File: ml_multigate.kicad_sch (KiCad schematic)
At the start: 3 parts, among them U1 4001, U2 1, U2 4001

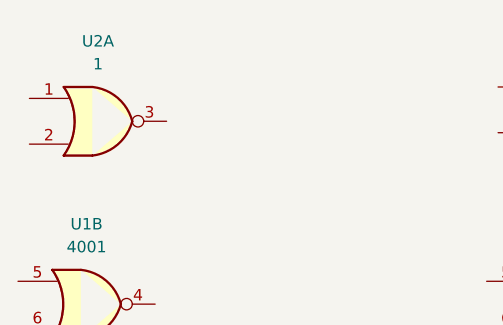
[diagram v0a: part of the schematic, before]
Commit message: Update ml_multigate.kicad_sch
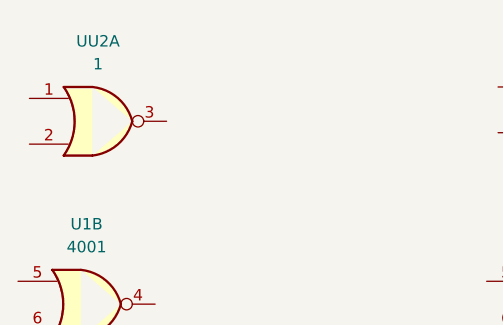
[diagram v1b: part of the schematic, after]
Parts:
- renumbered U2 to UU2
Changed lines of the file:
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@@
 		(dnp no)
 		(fields_autoplaced yes)
-		(property "Reference" "U2"
+		(property "Reference" "UU2"
 			(at 85.09 39.37 0)
 			(effects
